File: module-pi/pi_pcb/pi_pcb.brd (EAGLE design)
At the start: 65 x 56 mm, 8 parts, among them IC3 PIC16F870SO, K1 PIN20X2

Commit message: First pi hat PCB submitted.
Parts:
- removed IC3: PIC16F870SO, microchip:SO28W
- added JP5, JP6: (no value), pinhead:2X04
- moved JP4 0.50 mm to (14.8, 25.7)
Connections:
- removed net VDD: IC3.20
- removed net VSS: IC3.19, IC3.8
- new net +12V: IC2.14, JP1.2, JP5.2, JP6.2
- new net 0V: IC2.18, JP1.6, JP1.8
- new net GPIO13: JP6.5, K1.33
- new net GPIO6: JP5.5, K1.31
- new net ICSP_MCLR: IC2.1, JP4.1
- new net ICSP_PGC: IC2.5, JP4.5
- new net ICSP_PGD: IC2.4, JP4.4
- new net N$6: JP4.6
- new net STROBE+: JP1.7, JP1.9
- new net STROBE+_RES: IC2.15, JP1.5
- new net STROBE-: IC2.17, JP1.10
- new net STROBE_GATE: IC2.19
- new net STROBE_TRIG_IN: IC2.20, K1.29
- net +3V3: now also IC2.2, IC2.24, JP1.1, JP4.2, JP5.1, JP6.1
- net +5V: now also IC2.13, JP1.4, JP5.4, JP6.4
- net CE0: now also IC2.22
- net GND: now also IC2.23, IC2.3, JP1.3, JP4.3, JP5.3, JP6.3
- net MISO: now also IC2.28, JP5.8, JP6.8
- net MOSI: now also IC2.27, JP5.6, JP6.6
- net SCLK: now also IC2.26, JP5.7, JP6.7
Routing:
- net +3V3: track 0.00 -> 106.0 mm
- net +5V: track 0.00 -> 93.2 mm
- net MISO: track 0.00 -> 71.7 mm
- net MOSI: track 0.00 -> 69.2 mm
- net SCLK: track 0.00 -> 67.8 mm
- net GND: track 0.00 -> 54.9 mm
- net GPIO13: track 0.00 -> 33.8 mm
- net +12V: track 0.00 -> 33.4 mm
- net GPIO6: track 0.00 -> 23.7 mm
- net 0V: track 0.00 -> 22.4 mm
- net STROBE+_RES: track 0.00 -> 22.3 mm
- net CE0: track 0.00 -> 20.8 mm
- net STROBE_TRIG_IN: track 0.00 -> 17.8 mm
- net STROBE-: track 0.00 -> 16.3 mm
- net ICSP_MCLR: track 0.00 -> 4.68 mm
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
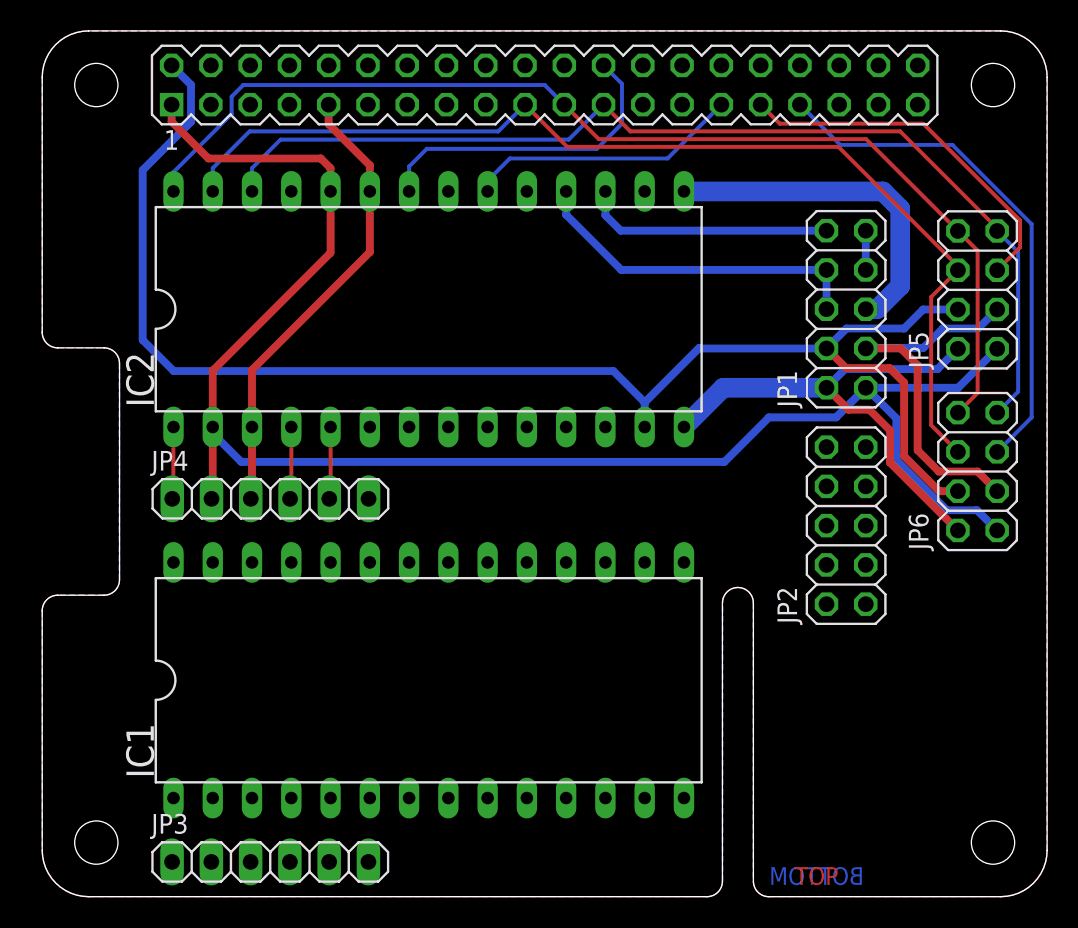
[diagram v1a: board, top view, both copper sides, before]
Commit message: Express order with 4-layer pressure/flow board.
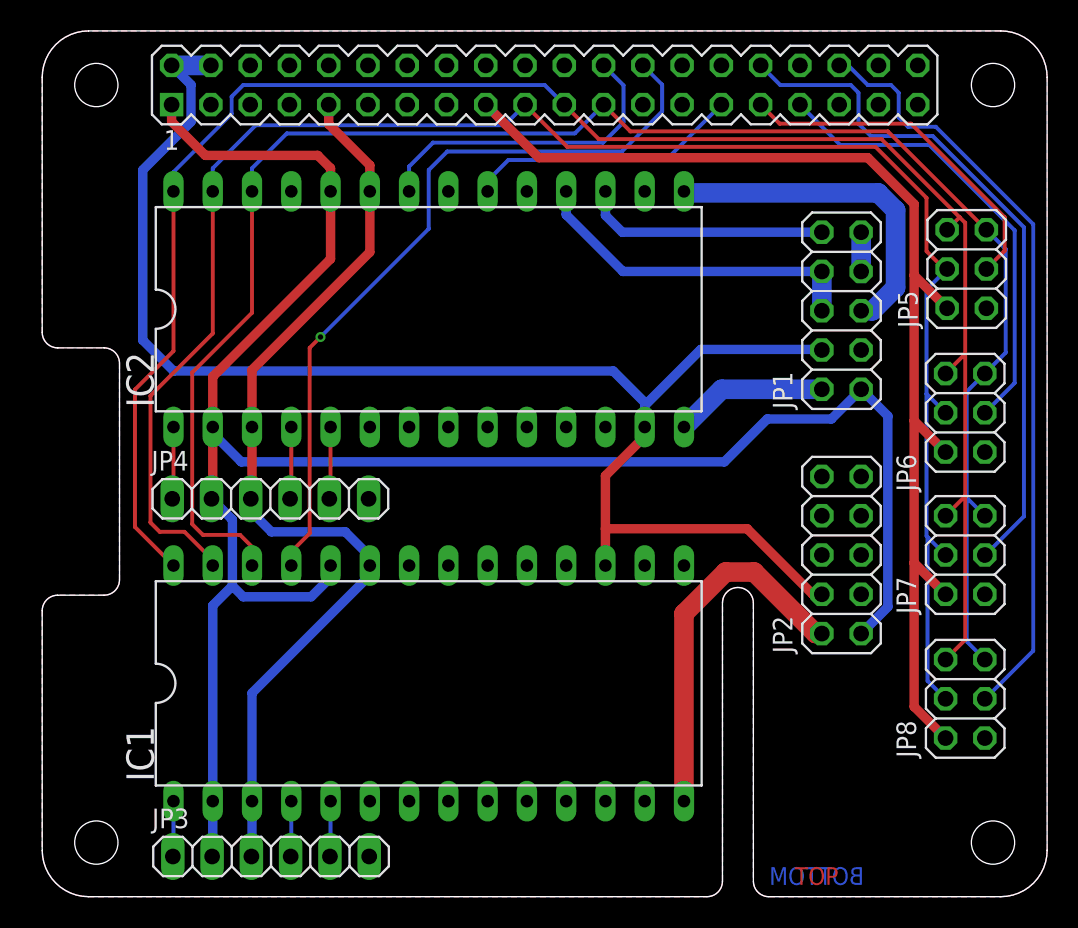
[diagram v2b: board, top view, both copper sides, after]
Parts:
- added JP7, JP8: (no value), pinhead:2X03
- JP5, JP6: device pinhead:2X04 -> pinhead:2X03
- moved JP6 3.88 mm to (59.7, 31.3)
- moved JP2 1.92 mm to (51.7, 22.1)
- moved JP5 1.52 mm to (59.8, 40.6)
- moved JP3 0.35 mm to (14.8, 2.60)
- moved JP1 0.32 mm to (51.7, 37.9)
- moved IC1 0.20 mm to (25.0, 13.8)
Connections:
- new net GPIO12: JP7.3, K1.32
- new net GPIO16: JP8.3, K1.36
- new net GPIO26: K1.37
- new net ICSP_MCLR2: IC2.1, JP4.1
- new net ICSP_PGC2: IC2.5, JP4.5
- new net ICSP_PGD2: IC2.4, JP4.4
- new net N$1: JP3.6
- net +12V: now also IC1.14, JP2.2; no longer JP5.2, JP6.2
- net +3V3: now also IC1.2, IC1.24, JP2.1, JP3.2, JP5.2, JP6.2, JP7.2, JP8.2; no longer JP5.1, JP6.1
- net +5V: now also IC1.17, JP2.4; no longer JP5.4, JP6.4
- net CE1: now also IC1.25
- net GND: now also IC1.13, IC1.23, IC1.3, JP2.3, JP3.3, JP5.1, JP6.1, JP7.1, JP8.1; no longer JP5.3, JP6.3
- net GPIO13: now also JP6.3; no longer JP6.5
- net GPIO6: now also JP5.3; no longer JP5.5
- net ICSP_MCLR: now also IC1.1, JP3.1; no longer IC2.1, JP4.1
- net ICSP_PGC: now also IC1.5, JP3.5; no longer IC2.5, JP4.5
- net ICSP_PGD: now also IC1.4, JP3.4; no longer IC2.4, JP4.4
- net MISO: now also IC1.28, JP5.6, JP6.6, JP7.6, JP8.6; no longer JP5.8, JP6.8
- net MOSI: now also IC1.27, JP5.4, JP6.4, JP7.4, JP8.4; no longer JP5.6, JP6.6
- net SCLK: now also IC1.26, JP5.5, JP6.5, JP7.5, JP8.5; no longer JP5.7, JP6.7
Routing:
- net +3V3: track 106.0 -> 206.2 mm
- net GPIO16: track 0.00 -> 49.8 mm
- net CE1: track 0.00 -> 49.4 mm, vias 0 -> 1
- net MOSI: track 69.2 -> 117.8 mm
- net MISO: track 71.7 -> 118.9 mm
- net SCLK: track 67.8 -> 114.4 mm
- net GPIO12: track 0.00 -> 44.8 mm
- net GND: track 54.9 -> 62.1 mm
- net ICSP_MCLR2: track 0.00 -> 4.68 mm
- net ICSP_PGD2: track 0.00 -> 4.68 mm
- net ICSP_PGC2: track 0.00 -> 4.68 mm
- net GPIO13: track 33.8 -> 29.9 mm
- net +5V: track 93.2 -> 96.6 mm
- net GPIO6: track 23.7 -> 22.6 mm
- net ICSP_PGD: track 4.68 -> 3.60 mm
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
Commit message: Module headers replaced.
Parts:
- removed IC1, IC2: (no value), ic-package:DIL28-6
- added X1, X2, X3, X4: SSW-114-02-G-S, con-samtec:SSW-114-02-G-S
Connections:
- net +12V: now also X1.14, X3.14; no longer IC1.14, IC2.14
- net +3V3: now also X1.2, X2.5, X3.2, X4.5; no longer IC1.2, IC1.24, IC2.2, IC2.24
- net +5V: now also X2.12, X3.13; no longer IC1.17, IC2.13
- net 0V: now also X4.11; no longer IC2.18
- net CE0: now also X4.7; no longer IC2.22
- net CE1: now also X2.4; no longer IC1.25
- net GND: now also X1.13, X1.3, X2.6, X3.3, X4.6; no longer IC1.13, IC1.23, IC1.3, IC2.23, IC2.3
- net ICSP_MCLR: now also X1.1; no longer IC1.1
- net ICSP_MCLR2: now also X3.1; no longer IC2.1
- net ICSP_PGC: now also X1.5; no longer IC1.5
- net ICSP_PGC2: now also X3.5; no longer IC2.5
- net ICSP_PGD: now also X1.4; no longer IC1.4
- net ICSP_PGD2: now also X3.4; no longer IC2.4
- net MISO: now also X2.1, X4.1; no longer IC1.28, IC2.28
- net MOSI: now also X2.2, X4.2; no longer IC1.27, IC2.27
- net SCLK: now also X2.3, X4.3; no longer IC1.26, IC2.26
- net STROBE+_RES: now also X4.14; no longer IC2.15
- net STROBE-: now also X4.12; no longer IC2.17
- net STROBE_GATE: now also X4.10; no longer IC2.19
- net STROBE_TRIG_IN: now also X4.9; no longer IC2.20

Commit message: Dedicated flow power 0V trace.
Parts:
- added JP9: (no value), pinhead:1X04
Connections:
- new net FLOW_+12V: JP2.2, X1.14
- new net FLOW_0V: JP2.6, JP2.8, X1.13
- net +12V: no longer JP2.2, X1.14
- net GND: now also JP9.1, JP9.2, JP9.3, JP9.4; no longer X1.13
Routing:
- net FLOW_0V: track 0.00 -> 29.0 mm
- net FLOW_+12V: track 0.00 -> 24.2 mm
- net +12V: track 33.7 -> 9.92 mm
- net STROBE+: track 2.54 -> 5.08 mm
- net 0V: track 22.1 -> 24.6 mm
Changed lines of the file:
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@@
 <attribute name="VALUE" x="44.685" y="44.33" size="1.27" layer="27" rot="R90"/>
+</element>
+<element name="JP9" library="pinhead" library_urn="urn:adsk.eagle:library:325" package="1X04" package3d_urn="urn:adsk.eagle:package:22407/2" value="" x="3" y="42.6" smashed="yes" rot="R90">
+<attribute name="NAME" x="1.1712" y="37.4438" size="1.27" layer="25" ratio="10" rot="R90"/>
+<attribute name="POPULARITY" value="91" x="3" y="42.6" size="1.778" layer="27" rot="R90" display="off"/>
+<attribute name="VALUE" x="6.175" y="37.52" size="1.27" layer="27" rot="R90"/>
 </element>
 </elements>
@@
 <wire x1="13.57" y1="2.64" x2="13.53" y2="2.6" width="0.6096" layer="16"/>
 <contactref element="X1" pad="3"/>
-<contactref element="X1" pad="13"/>
 <contactref element="X2" pad="6"/>
 <contactref element="X3" pad="3"/>
@@
 <wire x1="13.49" y1="25.735" x2="13.57" y2="25.815" width="0.508" layer="1"/>
 <wire x1="13.57" y1="25.815" x2="13.57" y2="30.4" width="0.508" layer="1"/>
+<contactref element="JP9" pad="4"/>
+<contactref element="JP9" pad="3"/>
+<contactref element="JP9" pad="2"/>
+<contactref element="JP9" pad="1"/>
 </signal>
 <signal name="+3V3">
@@
 <signal name="MOSI">
 <contactref element="K1" pad="19"/>
-<wire x1="13.81" y1="49.9" x2="11.155" y2="47.245" width="0.254" layer="16"/>
+<wire x1="13.81" y1="49.9" x2="11.03" y2="47.12" width="0.254" layer="16"/>
 <wire x1="13.81" y1="49.9" x2="29.9" y2="49.9" width="0.254" layer="16"/>
 <wire x1="29.9" y1="49.9" x2="31.23" y2="51.23" width="0.254" layer="16"/>
@@
 <wire x1="57.2" y1="41.75" x2="58.35" y2="40.6" width="0.254" layer="1"/>
 <wire x1="58.35" y1="40.6" x2="58.53" y2="40.6" width="0.254" layer="1"/>
-<wire x1="58.53" y1="40.6" x2="57.2" y2="39.27" width="0.254" layer="16"/>
-<wire x1="57.2" y1="32.53" x2="58.43" y2="31.3" width="0.254" layer="16"/>
-<wire x1="57.2" y1="39.27" x2="57.2" y2="32.53" width="0.254" layer="16"/>
+<wire x1="57.265" y1="32.465" x2="58.43" y2="31.3" width="0.254" layer="16"/>
 <contactref element="JP7" pad="4"/>
 <contactref element="JP8" pad="4"/>
@@
 <wire x1="7" y1="32.4" x2="7" y2="24.2" width="0.254" layer="1"/>
 <wire x1="11.03" y1="21.77" x2="9.2" y2="23.6" width="0.254" layer="1"/>
-<wire x1="57.2" y1="32.53" x2="57.2" y2="23.33" width="0.254" layer="16"/>
-<wire x1="57.2" y1="23.33" x2="57.265" y2="23.265" width="0.254" layer="16"/>
 <wire x1="57.265" y1="23.265" x2="58.43" y2="22.1" width="0.254" layer="16"/>
+<wire x1="57.265" y1="32.465" x2="57.265" y2="32" width="0.254" layer="16"/>
+<wire x1="57.265" y1="32" x2="57.265" y2="23.265" width="0.254" layer="16"/>
 <wire x1="57.265" y1="23.265" x2="57.265" y2="13.965" width="0.254" layer="16"/>
 <wire x1="57.265" y1="13.965" x2="58.43" y2="12.8" width="0.254" layer="16"/>
@@
 <wire x1="11.03" y1="21.4" x2="11.03" y2="21.77" width="0.254" layer="1"/>
 <wire x1="11.03" y1="36.43" x2="11.03" y2="45.6" width="0.254" layer="1"/>
-<wire x1="11.155" y1="47.245" x2="11.03" y2="47.12" width="0.254" layer="16"/>
 <wire x1="11.03" y1="47.12" x2="11.03" y2="45.6" width="0.254" layer="16"/>
+<wire x1="58.53" y1="40.6" x2="57.265" y2="39.335" width="0.254" layer="16"/>
+<wire x1="57.265" y1="39.335" x2="57.265" y2="32.465" width="0.254" layer="16"/>
 </signal>
 <signal name="MISO">
@@
 <contactref element="X4" pad="11"/>
 <wire x1="33.89" y1="44.11" x2="33.89" y2="45.6" width="0.6096" layer="16"/>
+<wire x1="50.43" y1="37.9" x2="50.43" y2="40.44" width="1.27" layer="1"/>
 </signal>
 <signal name="ICSP_MCLR">
@@
 <contactref element="JP1" pad="7"/>
 <wire x1="52.97" y1="42.98" x2="52.97" y2="40.44" width="1.27" layer="16"/>
+<wire x1="52.97" y1="40.44" x2="52.97" y2="42.98" width="1.27" layer="1"/>
 </signal>
 <signal name="STROBE-">
@@
 <signal name="+12V">
 <contactref element="JP1" pad="2"/>
-<contactref element="JP2" pad="2"/>
-<wire x1="50.43" y1="17.02" x2="50.03" y2="17.02" width="1.27" layer="1"/>
-<wire x1="50.03" y1="17.02" x2="46.05" y2="21" width="1.27" layer="1"/>
-<wire x1="46.05" y1="21" x2="44.2" y2="21" width="1.27" layer="1"/>
-<wire x1="41.51" y1="18.31" x2="44.2" y2="21" width="1.27" layer="1"/>
-<contactref element="X1" pad="14"/>
 <contactref element="X3" pad="14"/>
-<wire x1="41.51" y1="6.2" x2="41.51" y2="18.31" width="1.27" layer="1"/>
 <wire x1="43.93" y1="32.82" x2="41.51" y2="30.4" width="1.27" layer="16"/>
 <wire x1="50.43" y1="32.82" x2="43.93" y2="32.82" width="1.27" layer="16"/>
-<wire x1="50.43" y1="17.02" x2="50.43" y2="32.82" width="0" layer="19" extent="1-1"/>
 </signal>
 <signal name="STROBE+_RES">
@@
 <wire x1="55.4" y1="50.4" x2="56" y2="49.8" width="0.254" layer="16"/>
 <wire x1="56" y1="49.8" x2="57.8" y2="49.8" width="0.254" layer="16"/>
-<wire x1="57.8" y1="49.8" x2="64.1" y2="43.5" width="0.254" layer="16"/>
+<wire x1="64.1" y1="43.5" x2="57.8" y2="49.8" width="0.254" layer="16"/>
 <wire x1="64.1" y1="43.5" x2="64.1" y2="15.9" width="0.254" layer="16"/>
 <contactref element="JP8" pad="3"/>
@@
 <contactref element="K1" pad="37"/>
 </signal>
+<signal name="FLOW_0V">
+<contactref element="JP2" pad="6"/>
+<contactref element="JP2" pad="8"/>
+<contactref element="X1" pad="13"/>
+<wire x1="50.43" y1="22.1" x2="44.9" y2="22.1" width="1.27" layer="16"/>
+<wire x1="38.97" y1="16.17" x2="38.97" y2="6.2" width="1.27" layer="16"/>
+<wire x1="44.9" y1="22.1" x2="38.97" y2="16.17" width="1.27" layer="16"/>
+<wire x1="50.43" y1="22.1" x2="50.43" y2="24.64" width="1.27" layer="1"/>
+<wire x1="50.43" y1="22.1" x2="50.43" y2="24.64" width="1.27" layer="16"/>
+</signal>
+<signal name="FLOW_+12V">
+<contactref element="JP2" pad="2"/>
+<contactref element="X1" pad="14"/>
+<wire x1="46" y1="21.2" x2="44" y2="21.2" width="1.27" layer="1"/>
+<wire x1="44" y1="21.2" x2="41.51" y2="18.71" width="1.27" layer="1"/>
+<wire x1="41.51" y1="18.71" x2="41.51" y2="6.2" width="1.27" layer="1"/>
+<wire x1="49" y1="18.2" x2="48.5" y2="18.7" width="1.27" layer="1"/>
+<wire x1="48.5" y1="18.7" x2="46" y2="21.2" width="1.27" layer="1"/>
+<wire x1="49" y1="18.2" x2="50.18" y2="17.02" width="1.27" layer="1"/>
+<wire x1="50.18" y1="17.02" x2="50.43" y2="17.02" width="1.27" layer="1"/>
+</signal>
 </signals>

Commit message: External strobe trigger added.  Text and boxes added.
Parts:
- added JP10: (no value), pinhead:1X05
- added R1: (no value), rcl:R1206
- JP3, JP4: device pinhead:1X06 -> pinhead:1X05
- moved JP3 1.20 mm to (13.6, 2.60)
- moved JP4 1.20 mm to (13.6, 25.7)
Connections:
- removed net N$6: JP4.6
- new net STROBE_TRIG_PI: JP10.2, K1.29
- net +3V3: now also R1.1
- net GND: now also JP10.5
- net N$1: now also JP10.1, R1.2; no longer JP3.6
- net STROBE_TRIG_IN: now also JP10.3, JP10.4; no longer K1.29
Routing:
- net STROBE_TRIG_PI: track 0.00 -> 39.2 mm, vias 0 -> 1
- net STROBE_TRIG_IN: track 17.9 -> 23.0 mm
- net +3V3: track 206.2 -> 210.9 mm
- net N$1: track 0.00 -> 3.41 mm
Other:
- board text added: "Flow"
- board text added: "Heaters"
- board text added: "Pressure/Flow"
- board text added: "Strobe"

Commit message: Get and set sample holder power limit.
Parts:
- R1: value (none) -> 1k
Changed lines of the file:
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@@
 <?xml version="1.0" encoding="utf-8"?>
 <!DOCTYPE eagle SYSTEM "eagle.dtd">
-<eagle version="9.5.1">
+<eagle version="9.5.2">
 <drawing>
 <settings>
@@
 <attribute name="VALUE" x="23.35" y="22.625" size="1.27" layer="27"/>
 </element>
-<element name="R1" library="rcl" library_urn="urn:adsk.eagle:library:334" package="R1206" package3d_urn="urn:adsk.eagle:package:23540/2" value="" x="21.8" y="25.8" smashed="yes" rot="R90">
+<element name="R1" library="rcl" library_urn="urn:adsk.eagle:library:334" package="R1206" package3d_urn="urn:adsk.eagle:package:23540/2" value="1k" x="21.8" y="25.8" smashed="yes" rot="R90">
 <attribute name="NAME" x="20.53" y="24.53" size="1.27" layer="25" rot="R90"/>
 <attribute name="POPULARITY" value="41" x="21.8" y="25.8" size="1.778" layer="27" rot="R90" display="off"/>
